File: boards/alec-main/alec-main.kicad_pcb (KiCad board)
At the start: 4 copper layers, 64 x 56 mm, 125 parts, among them J1 Conn_01x02_Pin, J2 USB_C_Receptacle_USB2.0_16P, J3 Conn_01x02_Pin, J4 Conn_01x04_Pin, J5 BM07B-GHS-TBT, J6 BM06B-GHS-TBT, J7 UNPOPULATED_TEST_PADS, Q1 AO3401A, Q2 AO3401A, Q3 MMBT3904, Q4 MMBT3904, Q5 MMBT3904, Q6 AO3401A, Q7 MMBT3904, SW2 RESET, SW3 BOOT, U1 TPS63070RNMR, U2 TPS63070RNMR, U3 ESP32-S3-WROOM-1-N16, U4 USBLC6-2SC6, U5 RV-3028-C7, U6 MAX98357A, U7 SN74LVC2G66DCUR, U8 SN74LVC1T45DBVR

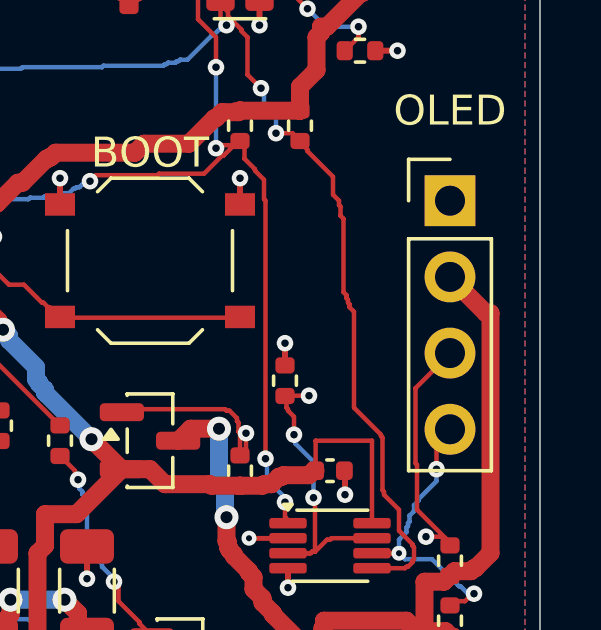
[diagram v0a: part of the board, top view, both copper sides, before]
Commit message: feat(rooster): consolidate the engineering baseline (#129)
* docs(rooster): start prototype order preparation and sourcing inventory

* docs(rooster): record JLCPCB quantities and assembly-side preflight

* docs(rooster): distinguish Beacon radar module from assembly socket

* feat(rooster): prepare sourced prototype BOM and complete placement drafts

* feat(rooster): validate prototype power parts and refine capacitor sourcing

* fix(rooster): synchronize assembly selections with native board sources

* feat(rooster): verify fabrication candidates and start supplier quote

* docs(rooster): require explicit approval before purchasing

* docs(rooster): record assembly quote and RTC sourcing options

* fix(rooster): correct controls placement centers and capture assembly quotes

* fix(rooster): correct header placements and capture four-board estimates

* docs(rooster): resolve amplifier copper pattern and stage production review

* docs(rooster): record LED fuse and header review findings

* docs(rooster): specify capped vias and verify mask clearance

* docs(rooster): verify mask bridges and prepare exact RTC preorder

* fix(rooster): allow finished-hole tolerance at main display header

* fab(rooster): export checked header-fit candidates and rebind placements

* Bind prototype via process attachments to current fabrication files

* Define prototype stackup and record USB functional-test disposition

* Record updated main quote with current Gerbers and fill-cap stackup

* docs(rooster): refresh Beacon quote and first-power handoff

* docs(rooster): prepare exact placement review and external inventory

* docs(rooster): define immediate order gates and prototype power scope

* docs(rooster): compare stocked RTC alternatives and compatibility

* docs(rooster): compare RTC manufacturers and enclosure thermal limits

* docs(rooster): compare PCB manufacturing and assembly suppliers

* docs(rooster): stage Cube first and retain JLCPCB recommendation

* docs(rooster): re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
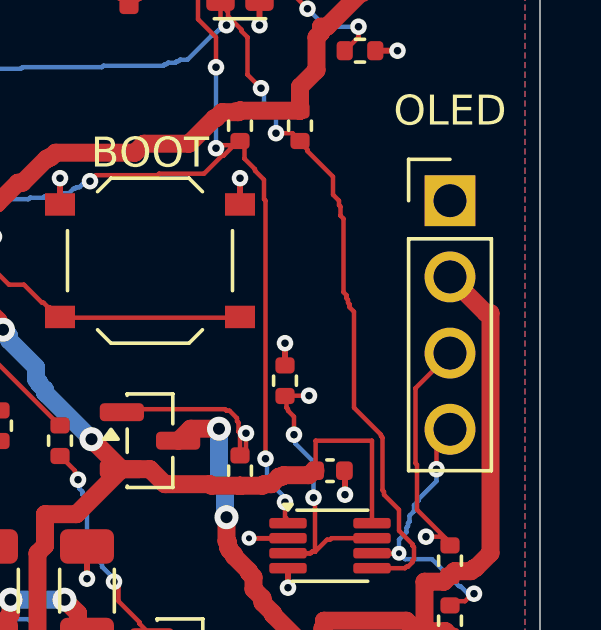
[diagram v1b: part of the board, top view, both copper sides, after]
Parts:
- J4: footprint Connector_PinHeader_2.54mm:PinHeader_1x04_P2.54mm_Vertical -> Board:Samtec_TSW-104-07-G-S_Drill1.10mm
